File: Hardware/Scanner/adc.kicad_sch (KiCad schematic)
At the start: 13 parts, among them U2 NAU7802SGI, X1 SG-8002CE

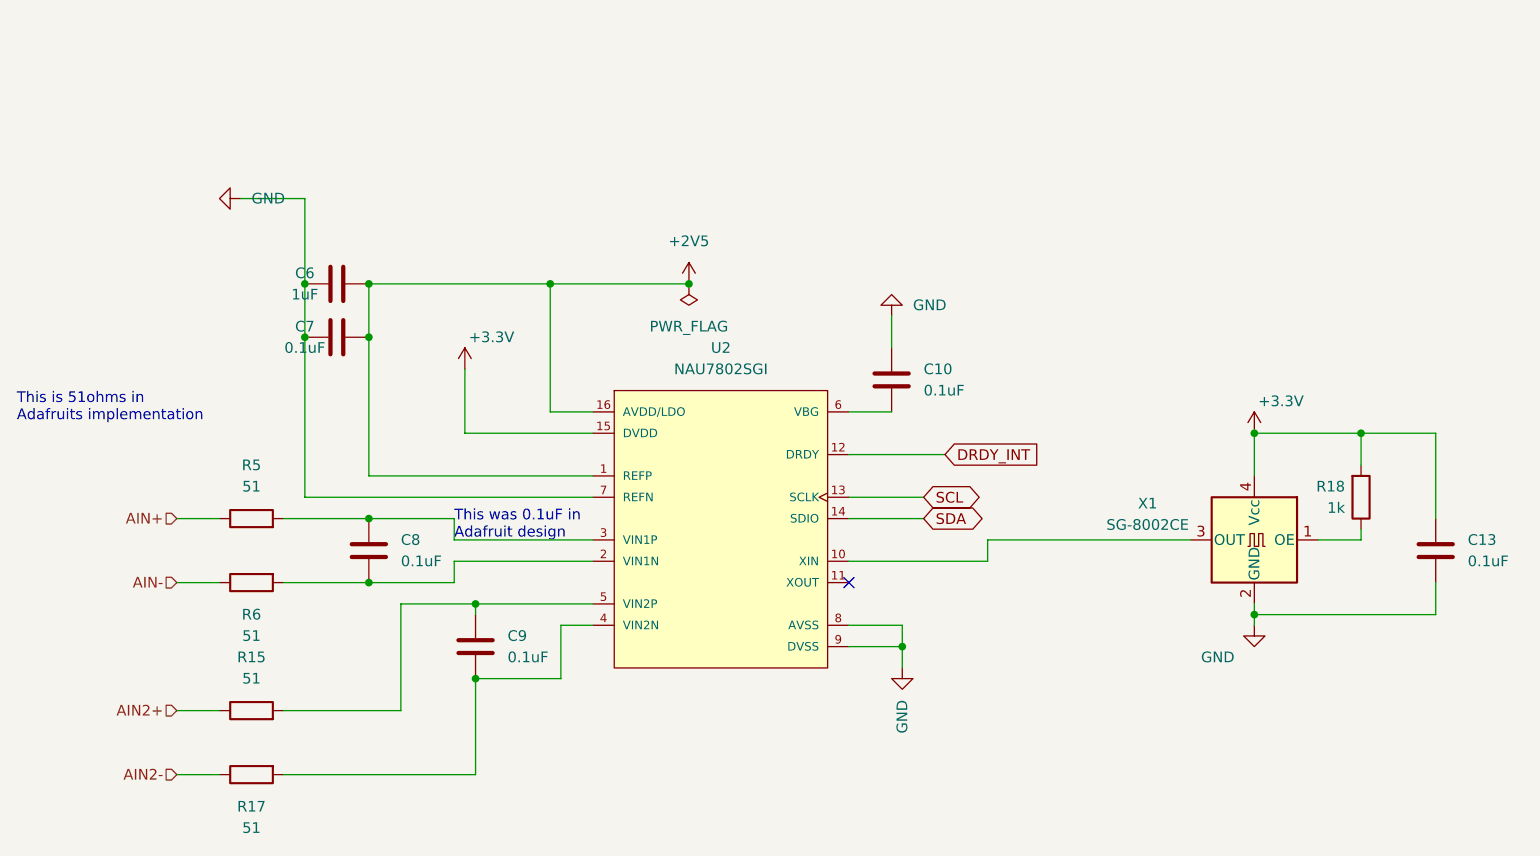
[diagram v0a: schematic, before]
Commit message: Updated LED and crystal descriptions
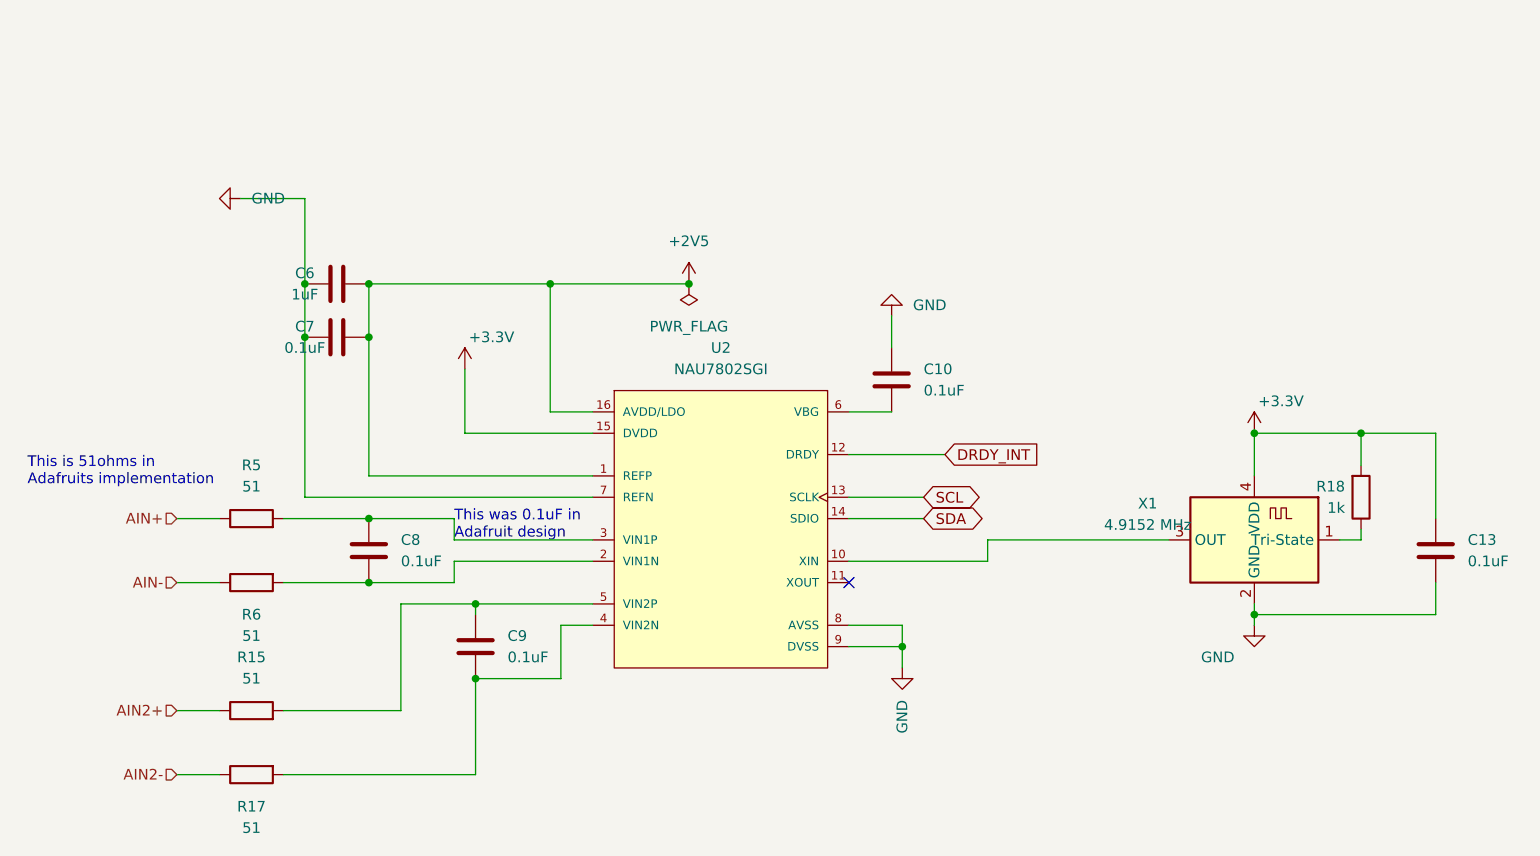
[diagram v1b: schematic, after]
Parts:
- X1: value SG-8002CE -> 4.9152 MHz; footprint Oscillator:Oscillator_SMD_SeikoEpson_SG8002CE-4Pin_3.2x2.5mm -> Oscillator:Oscillator_SMD_ECS_2520MV-xxx-xx-4Pin_2.5x2.0mm; symbol Oscillator:SG-8002CE -> Oscillator:ECS-2520MV-xxx-xx
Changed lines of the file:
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@@
+    (stroke (width 0) (type default) (color 0 0 0 0))
+  )
+  (wire (pts (xy 189.23 113.03) (xy 210.82 113.03))
     (stroke (width 0) (type default) (color 0 0 0 0))
   )
@@
     (stroke (width 0) (type default) (color 0 0 0 0))
   )
+  (wire (pts (xy 233.68 113.03) (xy 233.68 111.76))
+    (stroke (width 0) (type default) (color 0 0 0 0))
+  )
   (wire (pts (xy 105.41 110.49) (xy 115.57 110.49))
     (stroke (width 0) (type default) (color 0 0 0 0))
   )
-  (wire (pts (xy 233.68 111.76) (xy 233.68 113.03))
-    (stroke (width 0) (type default) (color 0 0 0 0))
-  )
   (wire (pts (xy 172.72 125.73) (xy 179.07 125.73))
     (stroke (width 0) (type default) (color 0 0 0 0))
@@
     (stroke (width 0) (type default) (color 0 0 0 0))
   )
-  (wire (pts (xy 233.68 113.03) (xy 228.6 113.03))
-    (stroke (width 0) (type default) (color 0 0 0 0))
-  )
   (wire (pts (xy 142.24 120.65) (xy 128.27 120.65))
     (stroke (width 0) (type default) (color 0 0 0 0))
@@
     (stroke (width 0) (type default) (color 0 0 0 0))
   )
+  (wire (pts (xy 231.14 113.03) (xy 233.68 113.03))
+    (stroke (width 0) (type default) (color 0 0 0 0))
+  )
   (wire (pts (xy 142.24 113.03) (xy 125.73 113.03))
     (stroke (width 0) (type default) (color 0 0 0 0))
@@
   )
   (wire (pts (xy 127 92.71) (xy 127 100.33))
-    (stroke (width 0) (type default) (color 0 0 0 0))
-  )
-  (wire (pts (xy 189.23 113.03) (xy 213.36 113.03))
     (stroke (width 0) (type default) (color 0 0 0 0))
   )
@@
     (effects (font (size 1.27 1.27)) (justify left bottom))
   )
-  (text "This is 51ohms in \nAdafruits implementation" (at 73.66 99.06 0)
+  (text "This is 51ohms in \nAdafruits implementation" (at 74.93 106.68 0)
     (effects (font (size 1.27 1.27)) (justify left bottom))
   )
@@
     (pin "2")
   )
-  (symbol (lib_id "Oscillator:SG-8002CE") (at 220.98 113.03 0) (mirror y) (unit 1)
+  (symbol (lib_id "Oscillator:ECS-2520MV-xxx-xx") (at 220.98 113.03 0) (mirror y) (unit 1)
     (in_bom yes) (on_board yes) (fields_autoplaced)
     (property "Reference" "X1" (id 0) (at 208.28 108.6993 0))
-    (property "Value" "SG-8002CE" (id 1) (at 208.28 111.2393 0))
-    (property "Footprint" "Oscillator:Oscillator_SMD_SeikoEpson_SG8002CE-4Pin_3.2x2.5mm" (id 2) (at 203.2 121.92 0)
-      (effects (font (size 1.27 1.27)) hide)
-    )
-    (property "Datasheet" "https://support.epson.biz/td/api/doc_check.php?mode=dl&lang=en&Parts=SG-8002DC" (id 3) (at 223.52 113.03 0)
-      (effects (font (size 1.27 1.27)) hide)
-    )
+    (property "Value" "4.9152 MHz" (id 1) (at 208.28 111.2393 0))
+    (property "Footprint" "Oscillator:Oscillator_SMD_ECS_2520MV-xxx-xx-4Pin_2.5x2.0mm" (id 2) (at 209.55 121.92 0)
+      (effects (font (size 1.27 1.27)) hide)
+    )
+    (property "Datasheet" "https://www.ecsxtal.com/store/pdf/ECS-2520MV.pdf" (id 3) (at 225.425 109.855 0)
+      (effects (font (size 1.27 1.27)) hide)
+    )

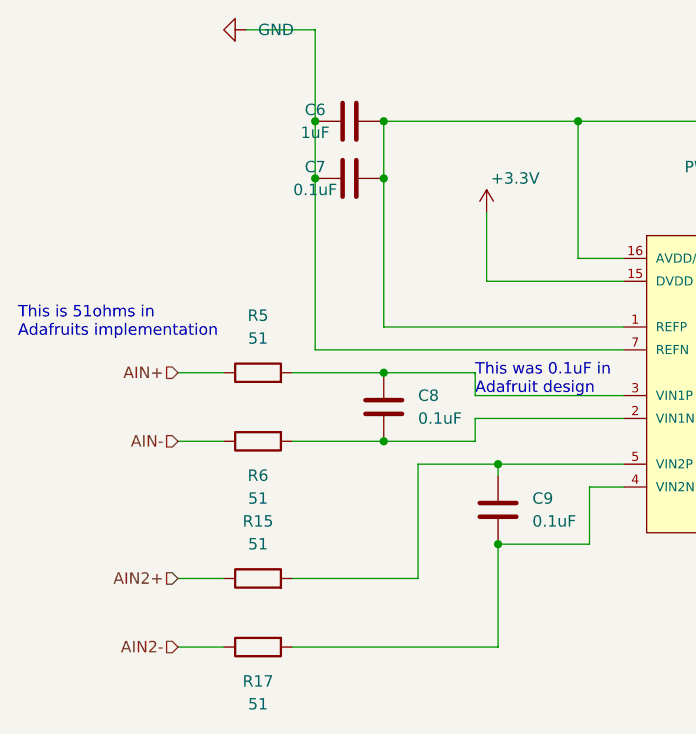
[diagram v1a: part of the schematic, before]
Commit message: Consistency of capacitor values
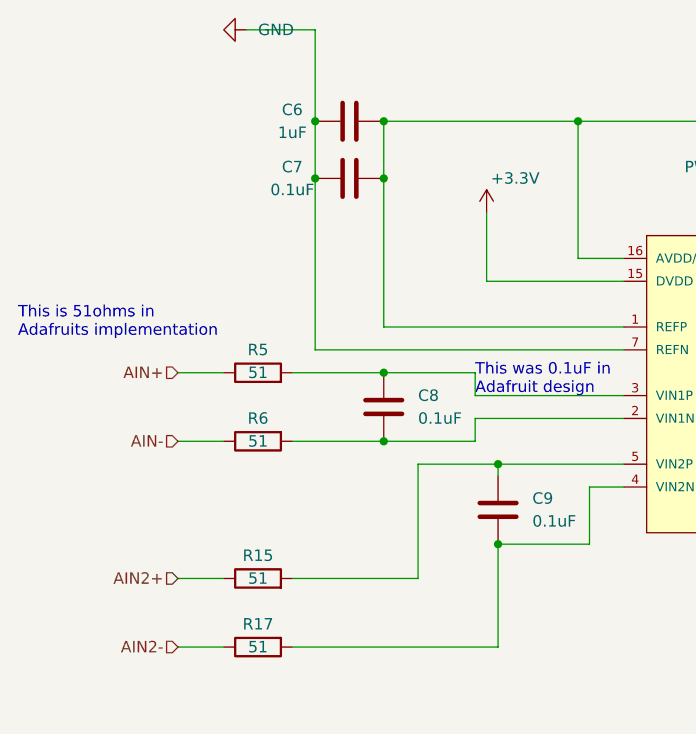
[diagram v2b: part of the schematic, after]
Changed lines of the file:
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@@
   (symbol (lib_id "Device:C") (at 111.76 82.55 90) (unit 1)
     (in_bom yes) (on_board yes)
-    (property "Reference" "C6" (id 0) (at 107.95 81.28 90))
-    (property "Value" "1uF" (id 1) (at 107.95 83.82 90))
+    (property "Reference" "C6" (id 0) (at 105.41 81.28 90))
+    (property "Value" "1uF" (id 1) (at 105.41 83.82 90))
     (property "Footprint" "Capacitor_SMD:C_0603_1608Metric_Pad1.08x0.95mm_HandSolder" (id 2) (at 115.57 81.5848 0)
       (effects (font (size 1.27 1.27)) hide)
@@
   (symbol (lib_id "Device:C") (at 111.76 88.9 90) (unit 1)
     (in_bom yes) (on_board yes)
-    (property "Reference" "C7" (id 0) (at 107.95 87.63 90))
-    (property "Value" "0.1uF" (id 1) (at 107.95 90.17 90))
+    (property "Reference" "C7" (id 0) (at 105.41 87.63 90))
+    (property "Value" "0.1uF" (id 1) (at 105.41 90.17 90))
     (property "Footprint" "Capacitor_SMD:C_0603_1608Metric_Pad1.08x0.95mm_HandSolder" (id 2) (at 115.57 87.9348 0)
       (effects (font (size 1.27 1.27)) hide)
@@
   (symbol (lib_id "Device:R") (at 101.6 140.97 90) (mirror x) (unit 1)
     (in_bom yes) (on_board yes)
-    (property "Reference" "R17" (id 0) (at 101.6 144.78 90))
-    (property "Value" "51" (id 1) (at 101.6 147.32 90))
+    (property "Reference" "R17" (id 0) (at 101.6 138.43 90))
+    (property "Value" "51" (id 1) (at 101.6 140.97 90))
     (property "Footprint" "Resistor_SMD:R_0603_1608Metric_Pad0.98x0.95mm_HandSolder" (id 2) (at 101.6 139.192 90)
       (effects (font (size 1.27 1.27)) hide)
@@
   )
   (symbol (lib_id "Device:R") (at 101.6 133.35 90) (unit 1)
-    (in_bom yes) (on_board yes) (fields_autoplaced)
-    (property "Reference" "R15" (id 0) (at 101.6 127 90))
-    (property "Value" "51" (id 1) (at 101.6 129.54 90))
+    (in_bom yes) (on_board yes)
+    (property "Reference" "R15" (id 0) (at 101.6 130.81 90))
+    (property "Value" "51" (id 1) (at 101.6 133.35 90))
     (property "Footprint" "Resistor_SMD:R_0603_1608Metric_Pad0.98x0.95mm_HandSolder" (id 2) (at 101.6 135.128 90)
       (effects (font (size 1.27 1.27)) hide)
@@
   (symbol (lib_id "Device:R") (at 101.6 118.11 90) (mirror x) (unit 1)
     (in_bom yes) (on_board yes)
-    (property "Reference" "R6" (id 0) (at 101.6 121.92 90))
-    (property "Value" "51" (id 1) (at 101.6 124.46 90))
+    (property "Reference" "R6" (id 0) (at 101.6 115.57 90))
+    (property "Value" "51" (id 1) (at 101.6 118.11 90))
     (property "Footprint" "Resistor_SMD:R_0603_1608Metric_Pad0.98x0.95mm_HandSolder" (id 2) (at 101.6 116.332 90)
       (effects (font (size 1.27 1.27)) hide)
@@
   )
   (symbol (lib_id "Device:R") (at 101.6 110.49 90) (unit 1)
-    (in_bom yes) (on_board yes) (fields_autoplaced)
-    (property "Reference" "R5" (id 0) (at 101.6 104.14 90))
-    (property "Value" "51" (id 1) (at 101.6 106.68 90))
+    (in_bom yes) (on_board yes)
+    (property "Reference" "R5" (id 0) (at 101.6 107.95 90))
+    (property "Value" "51" (id 1) (at 101.6 110.49 90))
     (property "Footprint" "Resistor_SMD:R_0603_1608Metric_Pad0.98x0.95mm_HandSolder" (id 2) (at 101.6 112.268 90)
       (effects (font (size 1.27 1.27)) hide)

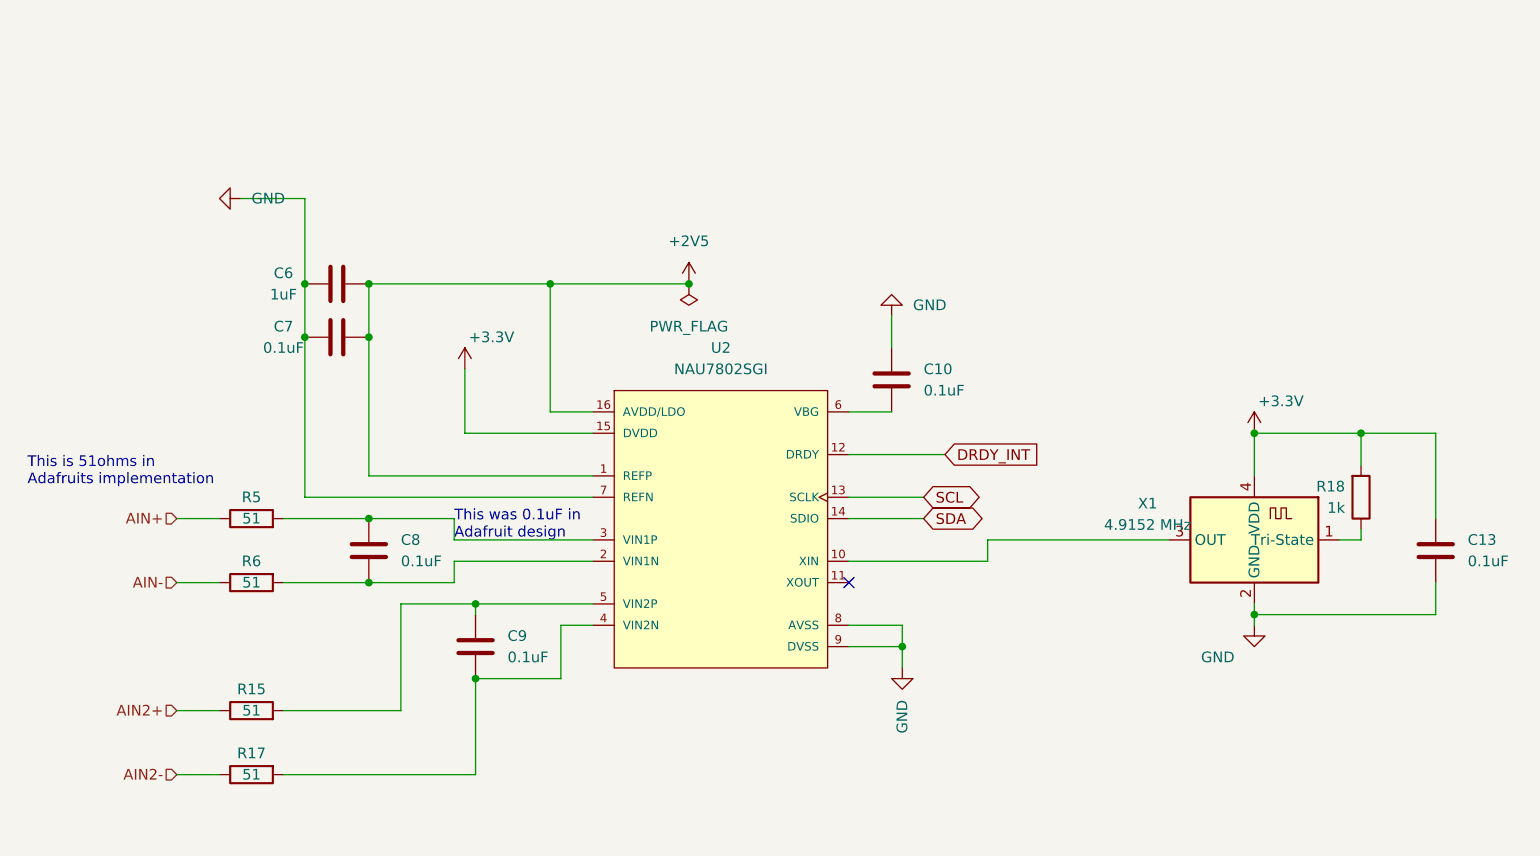
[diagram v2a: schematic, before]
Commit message: LAtching circuit for controller board + minors
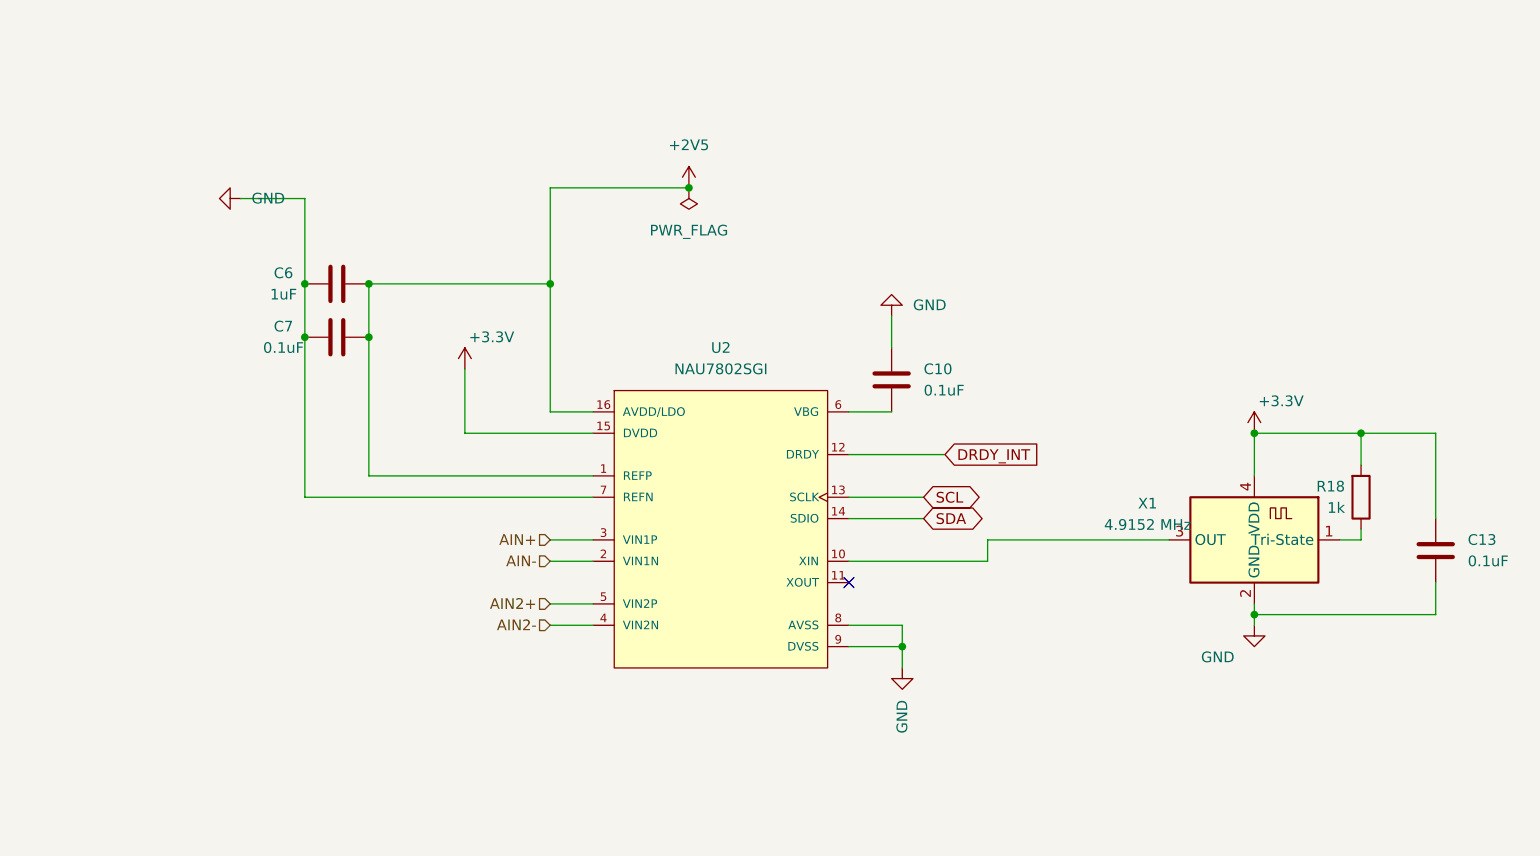
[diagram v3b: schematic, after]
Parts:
- removed C8, C9: 0.1uF, Capacitor_SMD:C_0603_1608Metric_Pad1.08x0.95mm_HandSolder, symbol Device:C
- removed R15, R17, R5, R6: 51, Resistor_SMD:R_0603_1608Metric_Pad0.98x0.95mm_HandSolder, symbol Device:R
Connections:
- net AIN+: now also U2.3 (VIN1P)
- net AIN-: now also U2.2 (VIN1N)
- net AIN2+: now also U2.5 (VIN2P)
- net AIN2-: now also U2.4 (VIN2N)
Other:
- note removed: "This is 51ohms in Adafruits implementation"
- note removed: "This was 0.1uF in Adafruit design"

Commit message: First commit - still a small error with compiling
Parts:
- added JP1: (no value), symbol Jumper:Jumper_2_Bridged
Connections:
- net +2V5: now also JP1.1 (A)
- net +3V3: now also JP1.2 (B)
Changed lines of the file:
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@@
   (junction (at 233.68 100.33) (diameter 0) (color 0 0 0 0)
+  )
+  (junction (at 137.16 71.12) (diameter 0) (color 0 0 0 0)
   )
   (junction (at 153.67 71.12) (diameter 0) (color 0 0 0 0)
@@
   )
   (wire (pts (xy 233.68 113.03) (xy 233.68 111.76))
+    (stroke (width 0) (type default) (color 0 0 0 0))
+  )
+  (wire (pts (xy 137.16 55.88) (xy 137.16 60.96))
     (stroke (width 0) (type default) (color 0 0 0 0))
   )
@@
     (pin "9")
   )
+  (symbol (lib_id "Jumper:Jumper_2_Bridged") (at 137.16 66.04 90) (unit 1)
+    (in_bom yes) (on_board yes) (fields_autoplaced)
+    (property "Reference" "JP1" (id 0) (at 138.43 64.7699 90)
+      (effects (font (size 1.27 1.27)) (justify right))
+    )
+    (property "Value" "" (id 1) (at 138.43 67.3099 90)
+      (effects (font (size 1.27 1.27)) (justify right))
+    )
+    (property "Footprint" "" (id 2) (at 137.16 66.04 0)
+      (effects (font (size 1.27 1.27)) hide)
+    )
+    (property "Datasheet" "~" (id 3) (at 137.16 66.04 0)
+      (effects (font (size 1.27 1.27)) hide)
+    )
+    (pin "1")
+    (pin "2")
+  )
   (symbol (lib_id "Device:R") (at 233.68 107.95 0) (mirror x) (unit 1)
     (in_bom yes) (on_board yes)
@@
     (pin "2")
   )
+  (symbol (lib_id "power:+3.3V") (at 137.16 55.88 0) (unit 1)
+    (in_bom yes) (on_board yes)
+    (property "Reference" "#PWR0135" (id 0) (at 137.16 59.69 0)
+      (effects (font (size 1.27 1.27)) hide)
+    )
+    (property "Value" "+3.3V" (id 1) (at 140.335 52.07 0))
+    (property "Footprint" "" (id 2) (at 137.16 55.88 0)
+      (effects (font (size 1.27 1.27)) hide)
+    )
+    (property "Datasheet" "" (id 3) (at 137.16 55.88 0)
+      (effects (font (size 1.27 1.27)) hide)
+    )
+    (pin "1")
+  )
   (symbol (lib_id "power:GND") (at 220.98 123.19 0) (mirror y) (unit 1)
